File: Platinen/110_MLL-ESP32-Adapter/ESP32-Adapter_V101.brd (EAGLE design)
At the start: 87.5 x 83.3 mm, 90 parts, among them IC1 ISO1050, J1.7 JUMPER-SMT_2_NO_SILK, J2.2 JUMPER-SMT_2_NO_SILK, J2.3 JUMPER-SMT_2_NO_SILK, J2.4 JUMPER-SMT_2_NO_SILK, J2.5 JUMPER-SMT_2_NO_SILK, J2.6 JUMPER-SMT_2_NO_SILK, J2.7 JUMPER-SMT_2_NO_SILK, J3.2 JUMPER-SMT_2_NO_SILK, J3.3 JUMPER-SMT_2_NO_SILK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

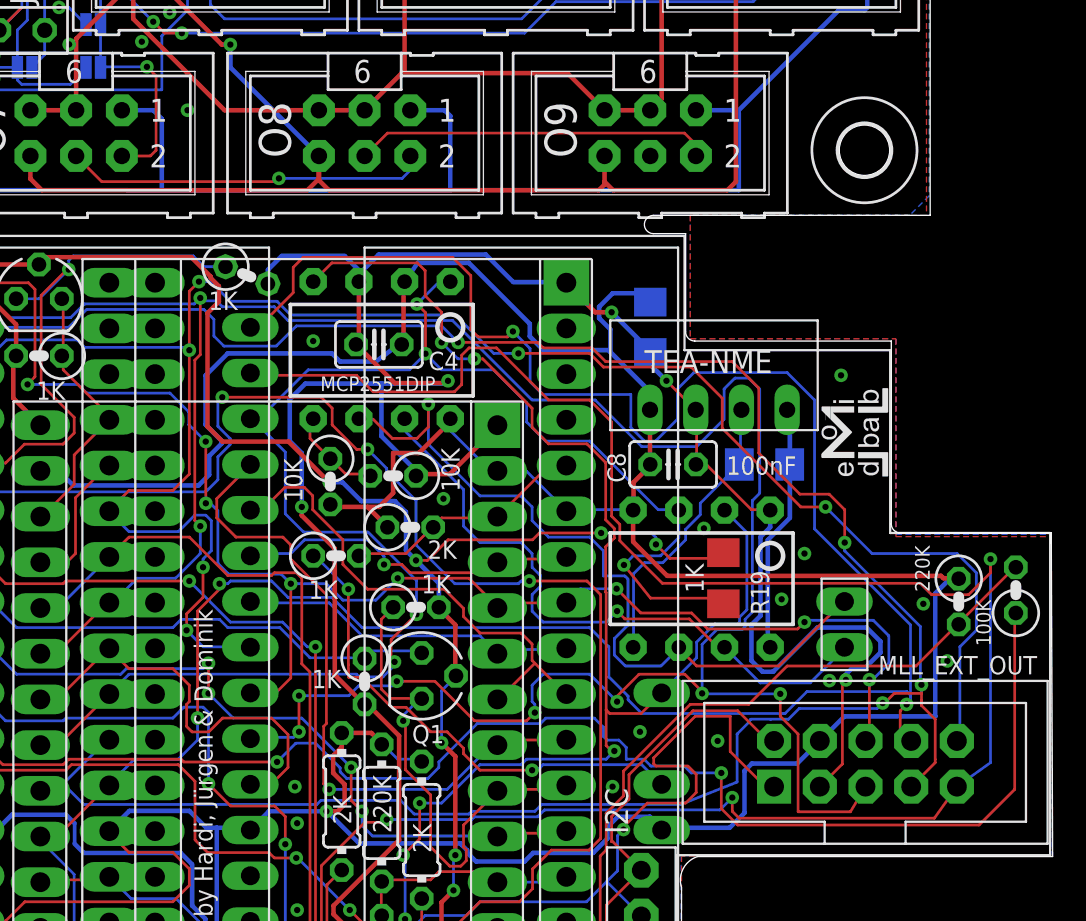
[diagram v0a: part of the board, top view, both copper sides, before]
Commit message: Update 110_MLL-ESP32-Adapter
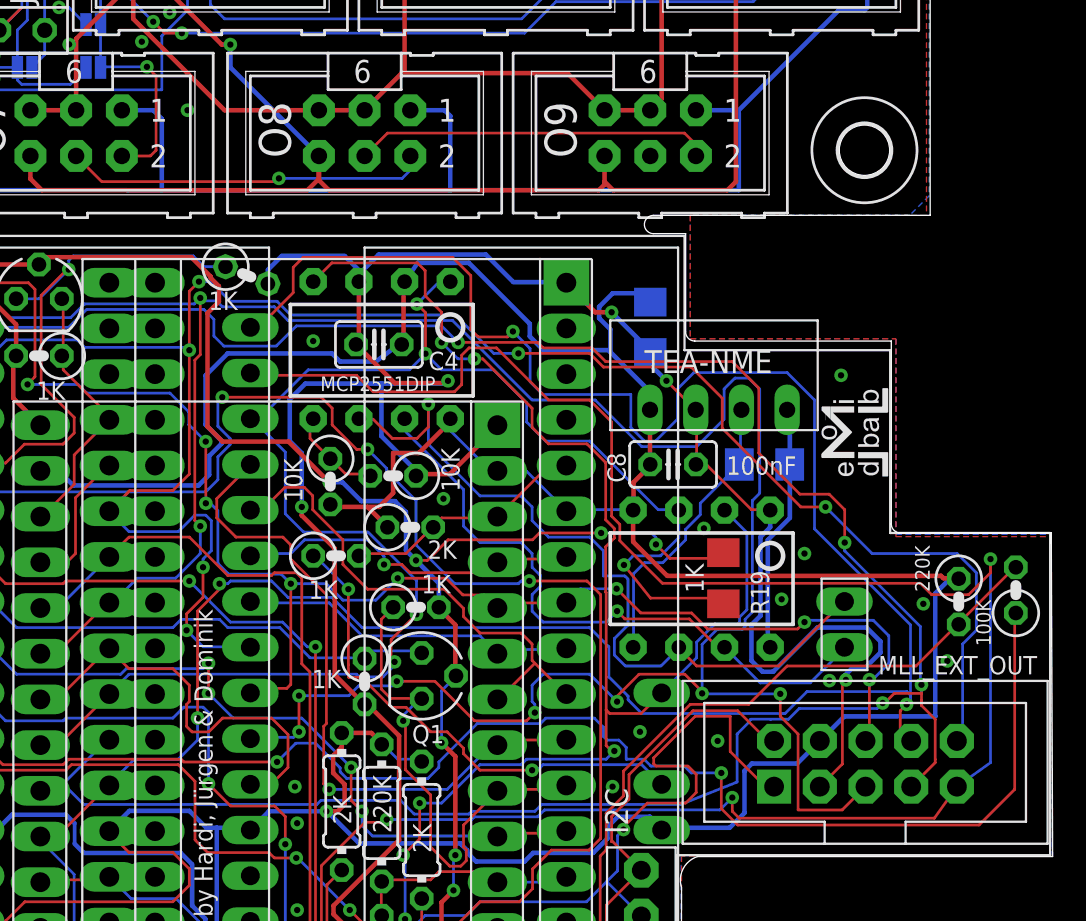
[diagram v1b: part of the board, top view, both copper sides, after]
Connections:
- net A2_HV renamed BUT_H
- net D12 renamed SWLEFT
- net D15 renamed CLOCK_L
- net D26 renamed SWMIDDLE
- net D27 renamed LED#0
- net D32 renamed LED#1
- net D33 renamed RESET_K_L
- net D34 renamed BUT_L
- net N$22 renamed RESET
- net N$3 renamed SWRIGHT
- net N$4 renamed CLOCK_H
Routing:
- net GND: track 627.6 -> 630.1 mm

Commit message: Updated Board-Files
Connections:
- removed net GND_1: U$1.CMD
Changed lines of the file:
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@@
 <rectangle x1="15.2273" y1="73.20915" x2="15.4178" y2="73.22185" layer="21"/>
 <rectangle x1="12.6238" y1="73.22185" x2="12.8016" y2="73.23455" layer="21"/>
-<text x="33.3502" y="0.5207" size="1.27" layer="21" font="vector">&gt;VERSION</text>
+<text x="56.8706" y="0.3429" size="1.016" layer="21" font="vector">&gt;VERSION</text>
 <text x="14.7066" y="12.5603" size="1.27" layer="21" font="vector" rot="R90">&gt;VERSION</text>
 <text x="79.06385" y="63.53175" size="1.27" layer="21" font="vector" rot="R180">&gt;VERSION</text>
-<text x="81.9023" y="19.64055" size="1.27" layer="22" font="vector" rot="MR180">&gt;VERSION</text>
-<text x="18.95475" y="82.2579" size="1.27" layer="22" font="vector" rot="MR180">&gt;VERSION</text>
-<text x="80.09255" y="82.86115" size="1.27" layer="22" font="vector" rot="MR270">&gt;DATUM</text>
+<text x="81.3181" y="20.25015" size="1.27" layer="22" font="vector" rot="MR180">&gt;VERSION</text>
+<text x="17.07515" y="82.4103" size="1.27" layer="22" font="vector" rot="MR180">&gt;VERSION</text>
+<text x="79.10195" y="82.42935" size="1.27" layer="22" font="vector" rot="MR270">&gt;DATUM</text>
 <text x="79.5909" y="64.0842" size="1.27" layer="22" font="vector" rot="MR270">&gt;VERSION</text>
 <text x="1.16205" y="82.27695" size="1.27" layer="22" font="vector" rot="MR180">&gt;DATUM</text>
-<text x="31.48965" y="2.45745" size="1.27" layer="22" font="vector" rot="MR180">&gt;DATUM</text>
-<text x="63.119" y="2.83845" size="0.8128" layer="21" font="vector" rot="R90">&gt;DATUM</text>
+<text x="69.91985" y="20.36445" size="1.27" layer="22" font="vector" rot="MR180">&gt;DATUM</text>
+<text x="62.8396" y="0.70485" size="0.8128" layer="21" font="vector" rot="R90">&gt;DATUM</text>
 <text x="10.64895" y="73.62825" size="1.27" layer="21" font="vector" rot="R180">&gt;DATUM</text>
 <text x="80.4291" y="61.8744" size="1.27" layer="21" font="vector" rot="R180">&gt;DATUM</text>
-<text x="79.883" y="72.517" size="1.778" layer="22" rot="MR0">Hauptplatine ESP32 Adapter</text>
-<text x="86.741" y="24.638" size="1.778" layer="22" rot="MR0">Hauptplatine
+<text x="79.121" y="72.517" size="1.778" layer="22" rot="MR0">Hauptplatine ESP32 Adapter</text>
+<text x="86.4362" y="25.6032" size="1.4224" layer="22" rot="MR0">Hauptplatine
 ESP32 Adapter</text>
 <text x="15.494" y="57.277" size="1.778" layer="22" rot="MR270">Hauptplatine ESP32 Adapter</text>
 <text x="13.081" y="53.848" size="1.27" layer="22" rot="MR270">by Hardi, Jürgen, Dominik </text>
-<text x="62.484" y="1.27" size="1.27" layer="22" rot="MR0">by Hardi, Jürgen, Dominik </text>
-<text x="53.848" y="72.263" size="1.27" layer="22" rot="MR180">by Hardi, Jürgen, Dominik </text>
+<text x="60.833" y="1.1176" size="1.27" layer="22" rot="MR0">by Hardi, Jürgen, Dominik </text>
+<text x="52.1462" y="71.9836" size="1.27" layer="22" rot="MR180">by Hardi, Jürgen, Dominik </text>
 <text x="40.767" y="14.859" size="1.016" layer="21" rot="R90">by Hardi, Jürgen &amp; Dominik </text>
-<text x="58.293" y="1.397" size="1.016" layer="21" rot="R180">Hauptplatine ESP32 Adapter</text>
+<text x="51.2318" y="1.3208" size="1.016" layer="21" rot="R180">Hauptplatine ESP32 Adapter</text>
 <wire x1="24.4094" y1="3.7846" x2="24.3332" y2="77.3684" width="0.3048" layer="51"/>
 <wire x1="64.7446" y1="53.2638" x2="24.3586" y2="53.2638" width="0.3048" layer="51"/>
 </plain>
 <attributes>
-<attribute name="DATUM" value="04/2021"/>
+<attribute name="DATUM" value="05/2021"/>
 <attribute name="VERSION" value="V1.0.1"/>
 </attributes>
@@
 </signal>
 <signal name="GND_1">
-<contactref element="U$1" pad="CMD"/>
 </signal>
 </signals>
